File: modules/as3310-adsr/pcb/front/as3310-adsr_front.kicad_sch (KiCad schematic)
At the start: 21 parts

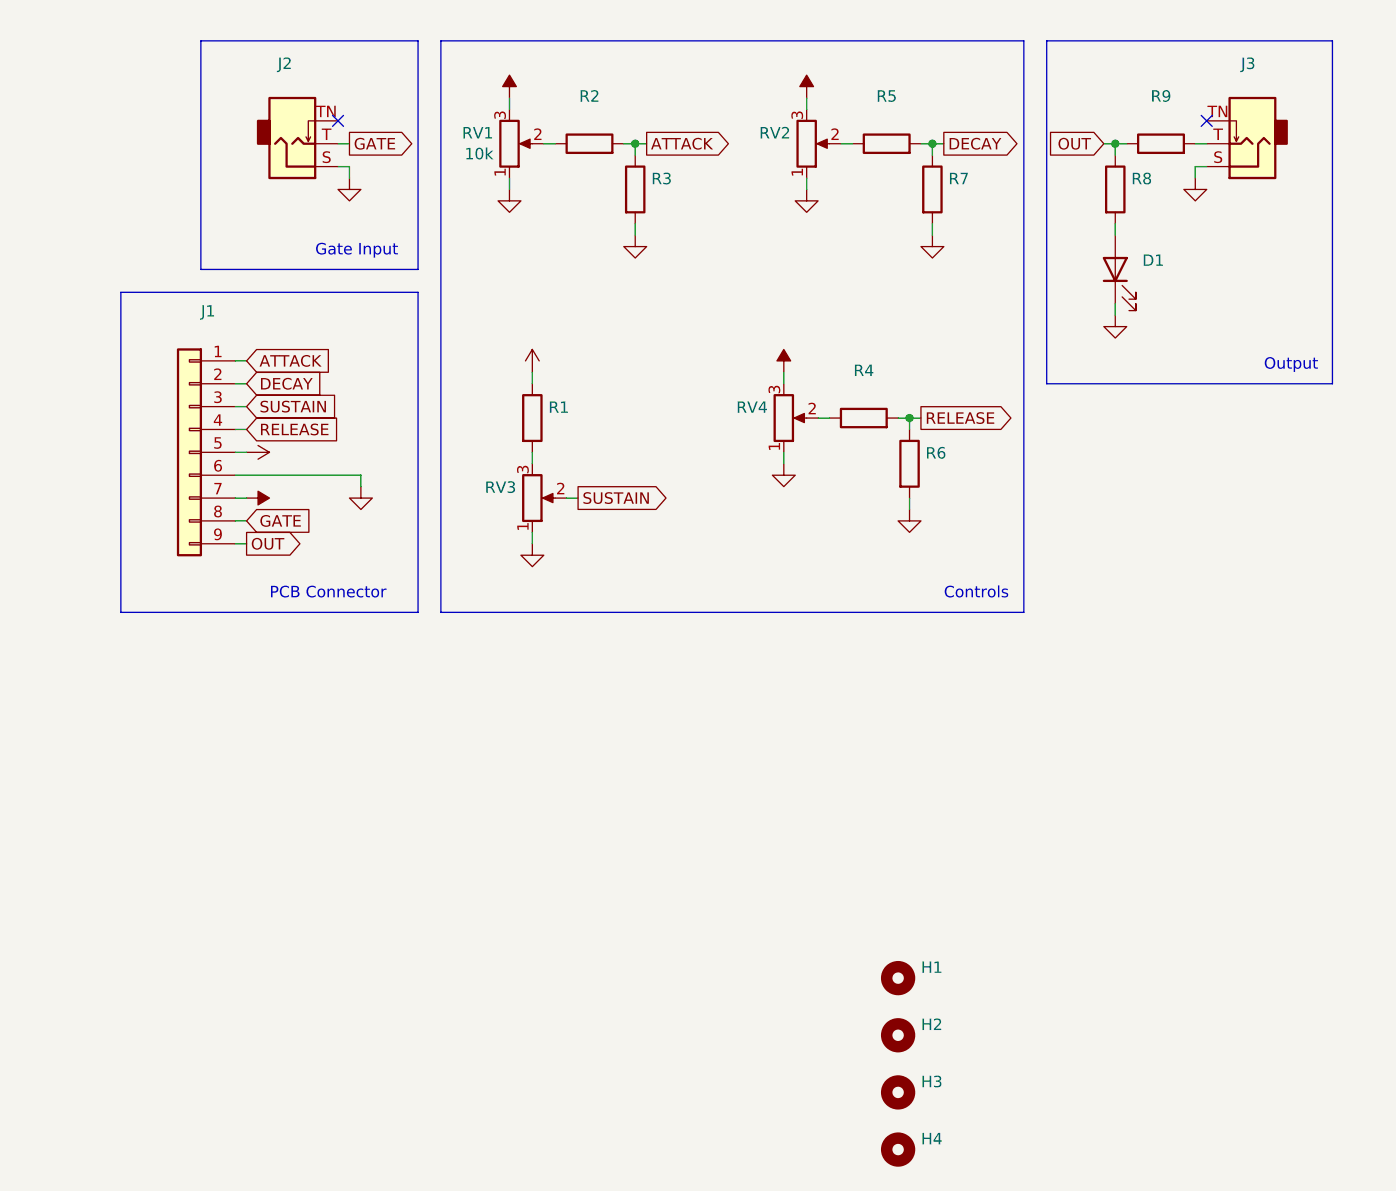
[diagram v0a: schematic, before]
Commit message: modules: as3310-adsr: front: revision A (redesign)
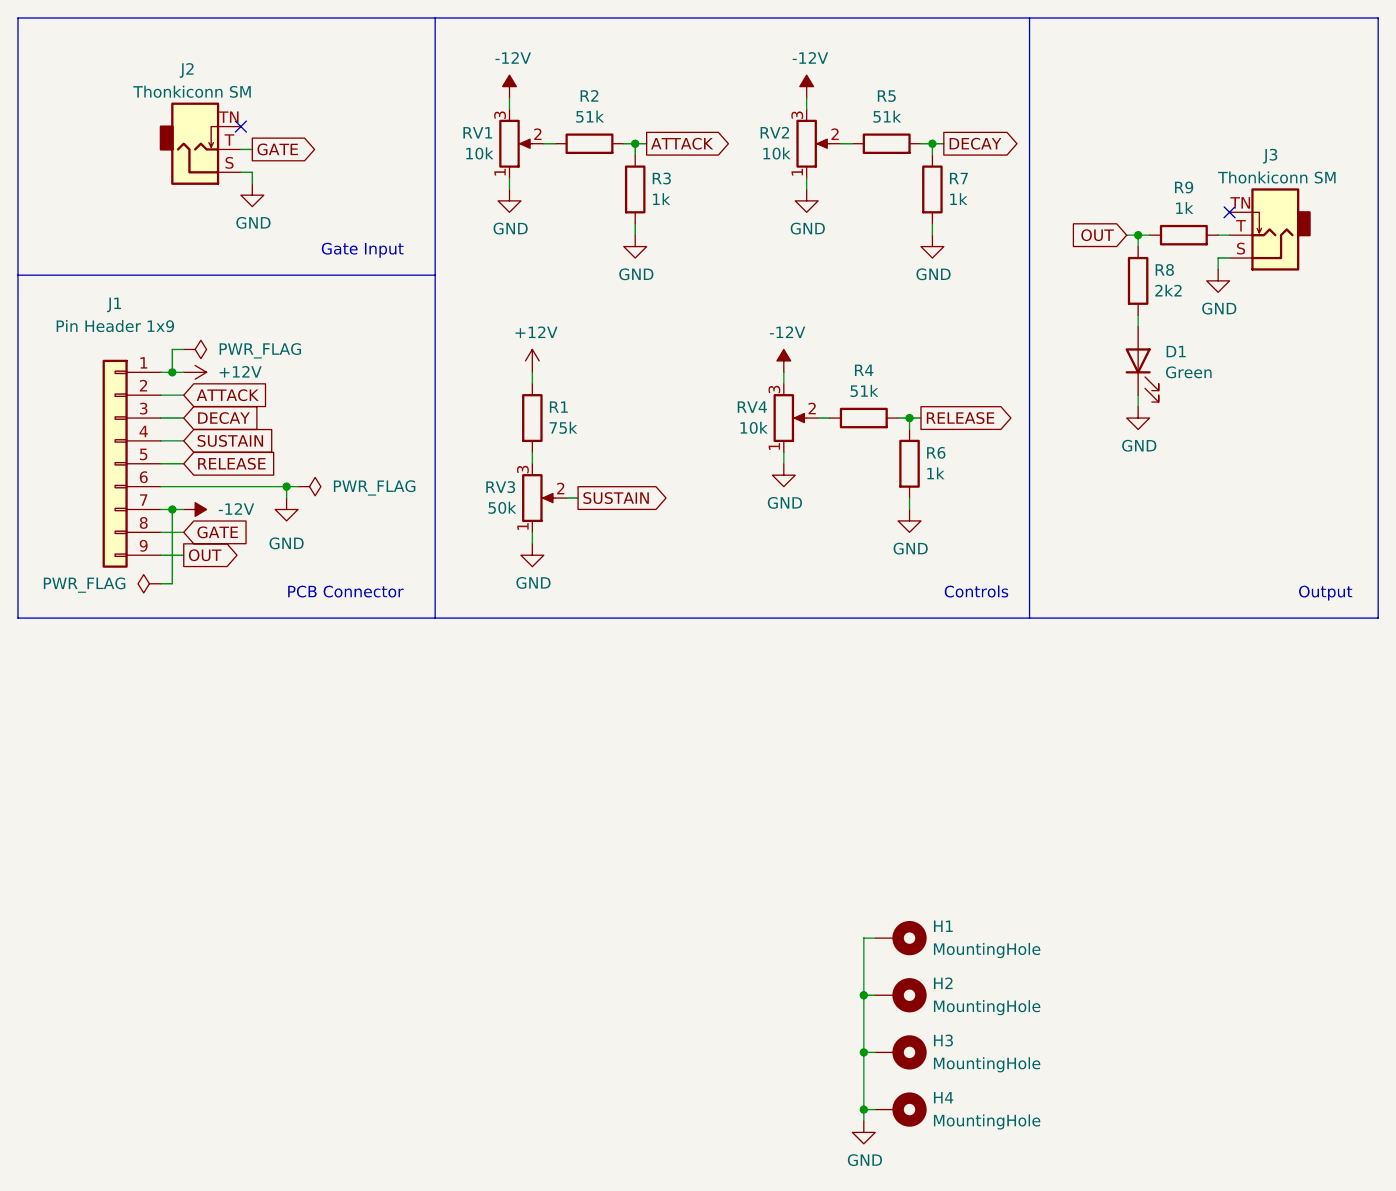
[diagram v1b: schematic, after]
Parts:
- D1: value (none) -> Green; footprint (none) -> LED_THT:LED_D3.0mm
- H1, H2, H3, H4: value (none) -> MountingHole; footprint (none) -> MountingHole:MountingHole_2.2mm_M2_Pad_Via; symbol Mechanical:MountingHole -> Mechanical:MountingHole_Pad
- J1: value (none) -> Pin Header 1x9; footprint (none) -> Connector_PinHeader_2.54mm:PinHeader_1x09_P2.54mm_Vertical
- J2, J3: value (none) -> Thonkiconn SM; footprint (none) -> eurorack:Jack_3.5mm_QingPu_WQP-PJ398SM_Vertical
- R1: value (none) -> 75k; footprint (none) -> Resistor_THT:R_Axial_DIN0207_L6.3mm_D2.5mm_P10.16mm_Horizontal
- R2, R4, R5: value (none) -> 51k; footprint (none) -> Resistor_THT:R_Axial_DIN0207_L6.3mm_D2.5mm_P10.16mm_Horizontal
- R3, R6, R7, R9: value (none) -> 1k; footprint (none) -> Resistor_THT:R_Axial_DIN0207_L6.3mm_D2.5mm_P10.16mm_Horizontal
- R8: value (none) -> 2k2; footprint (none) -> Resistor_THT:R_Axial_DIN0207_L6.3mm_D2.5mm_P10.16mm_Horizontal
- RV2, RV4: value (none) -> 10k; footprint (none) -> Potentiometer_THT:Potentiometer_Alpha_RD901F-40-00D_Single_Vertical_CircularHoles
- RV3: value (none) -> 50k; footprint (none) -> Potentiometer_THT:Potentiometer_Alpha_RD901F-40-00D_Single_Vertical_CircularHoles
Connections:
- net +12V: now also J1.1 (Pin_1); no longer J1.5 (Pin_5)
- net ATTACK: now also J1.2 (Pin_2); no longer J1.1 (Pin_1)
- net DECAY: now also J1.3 (Pin_3); no longer J1.2 (Pin_2)
- net GND: now also H1.1, H2.1, H3.1, H4.1
- net RELEASE: now also J1.5 (Pin_5); no longer J1.4 (Pin_4)
- net SUSTAIN: now also J1.4 (Pin_4); no longer J1.3 (Pin_3)
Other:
- company: (none) -> eurorack.rgm.io
- moved on the sheet: D1, J1, J2, J3, R8, R9
